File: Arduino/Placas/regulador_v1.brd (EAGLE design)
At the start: 5 parts

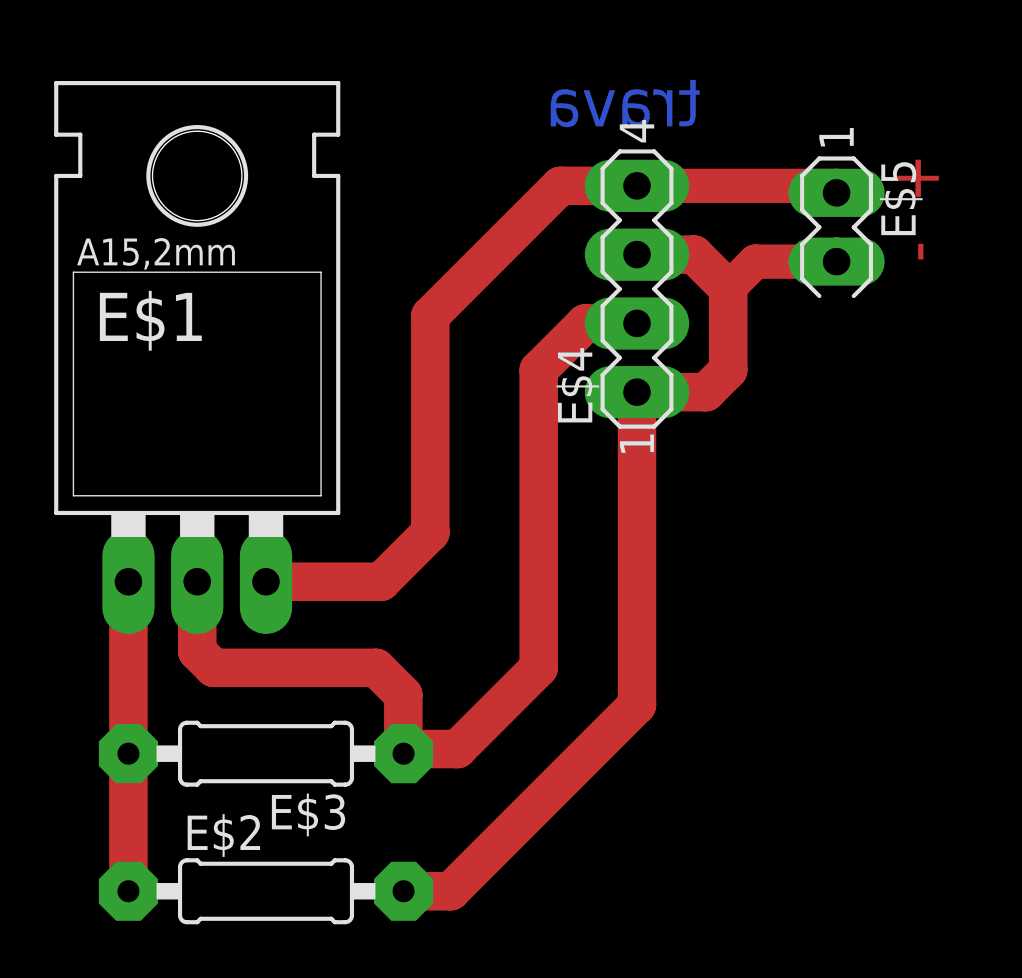
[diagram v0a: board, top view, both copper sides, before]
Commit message: Restored regulator board
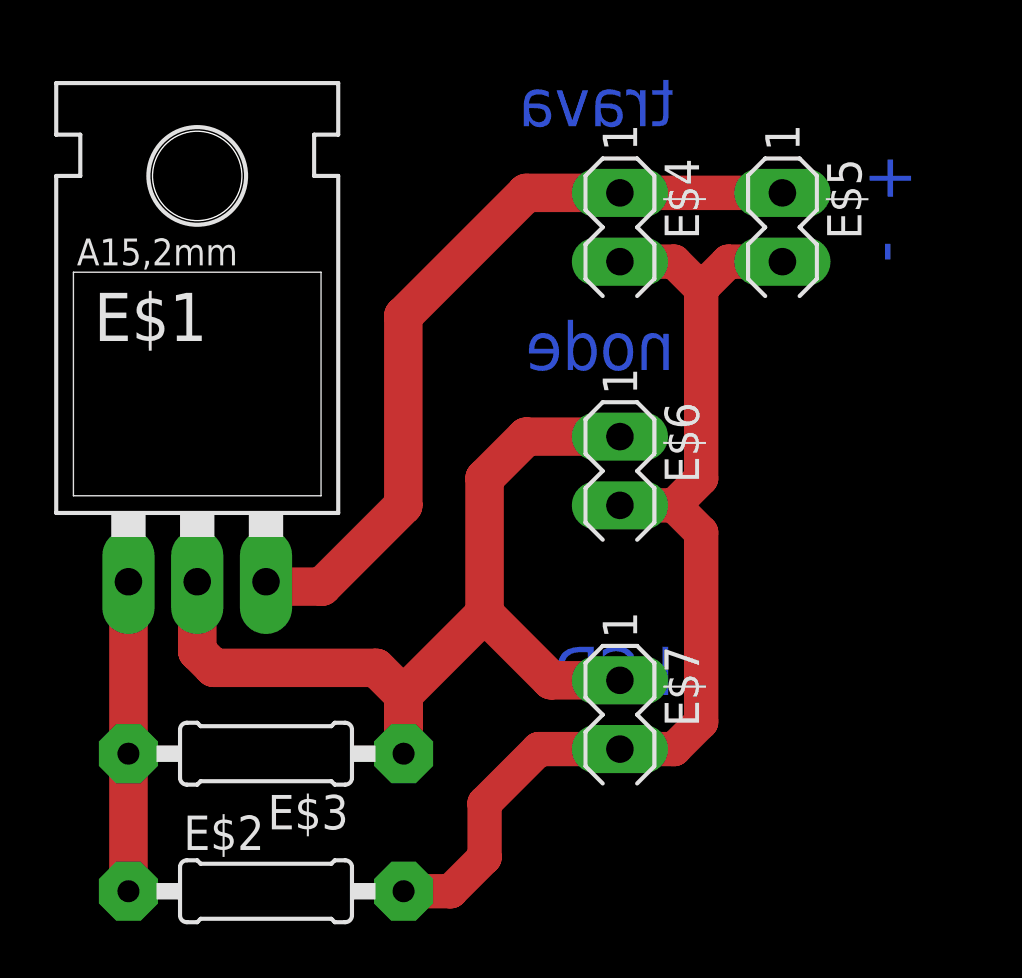
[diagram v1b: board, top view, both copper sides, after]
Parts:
- added E$6, E$7: (no value), con-lstb:MA03-1
- E$4: device con-lstb:MA04-1 -> con-lstb:MA03-1
- moved E$5 2.00 mm to (94.0, 55.0)
- moved E$4 1.19 mm to (88.0, 55.0), turned to 270 degrees
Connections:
- net S$2: now also E$6.1, E$7.1; no longer E$4.2
- net S$3: now also E$4.2, E$6.2, E$7.2; no longer E$4.1, E$4.3, E$5.2
- net S$4: now also E$4.1; no longer E$4.4
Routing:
- net S$4: track 32.1 -> 29.3 mm
- net S$3: track 38.4 -> 40.4 mm
- net S$2: track 34.5 -> 36.2 mm
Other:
- board text added: "LCD"
- board text added: "node"
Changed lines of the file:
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@@
 <board>
 <plain>
-<text x="98" y="59" size="1.778" layer="1" rot="R270">-  +</text>
-<text x="91" y="60" size="1.778" layer="16" rot="MR0">trava</text>
+<text x="90" y="60" size="1.778" layer="16" rot="MR0">trava</text>
+<text x="90" y="51" size="1.778" layer="16" rot="MR0">node</text>
+<text x="90" y="39" size="1.778" layer="16" rot="MR0">LCD
+</text>
+<text x="99" y="59" size="1.778" layer="16" rot="MR270">-  +</text>
 </plain>
 <attributes>
@@
 <element name="E$2" library="eagle-ltspice" package="0207/10" value="" x="74.93" y="31.75"/>
 <element name="E$3" library="eagle-ltspice" package="0207/10" value="" x="74.93" y="36.83" rot="R180"/>
-<element name="E$4" library="con-lstb" package="MA04-1" value="" x="88.63" y="53.99" rot="R90"/>
-<element name="E$5" library="con-lstb" package="MA03-1" value="" x="96" y="55" rot="R270"/>
+<element name="E$5" library="con-lstb" package="MA03-1" value="" x="94" y="55" rot="R270"/>
+<element name="E$4" library="con-lstb" package="MA03-1" value="" x="88" y="55" rot="R270"/>
+<element name="E$6" library="con-lstb" package="MA03-1" value="" x="88" y="46" rot="R270"/>
+<element name="E$7" library="con-lstb" package="MA03-1" value="" x="88" y="37" rot="R270"/>
 </elements>
 <signals>
@@
 <wire x1="69.85" y1="31.75" x2="69.85" y2="36.83" width="1.4224" layer="1"/>
 </signal>
+<signal name="S$4">
+<contactref element="E$5" pad="1"/>
+<contactref element="E$4" pad="1"/>
+<contactref element="E$1" pad="3"/>
+<wire x1="88" y1="57.54" x2="94" y2="57.54" width="1.27" layer="1"/>
+<wire x1="88" y1="57.54" x2="84.54" y2="57.54" width="1.4224" layer="1"/>
+<wire x1="84.54" y1="57.54" x2="80" y2="53" width="1.4224" layer="1"/>
+<wire x1="80" y1="53" x2="80" y2="46" width="1.4224" layer="1"/>
+<wire x1="80" y1="46" x2="77" y2="43" width="1.4224" layer="1"/>
+<wire x1="77" y1="43" x2="75.11" y2="43" width="1.4224" layer="1"/>
+<wire x1="75.11" y1="43" x2="74.93" y2="43.18" width="1.4224" layer="1"/>
+</signal>
 <signal name="S$2">
+<contactref element="E$6" pad="1"/>
+<wire x1="88" y1="48.54" x2="84.54" y2="48.54" width="1.4224" layer="1"/>
+<wire x1="83" y1="47" x2="84.54" y2="48.54" width="1.4224" layer="1"/>
+<wire x1="83" y1="42" x2="83" y2="47" width="1.4224" layer="1"/>
+<contactref element="E$3" pad="1"/>
+<wire x1="80.18" y1="37" x2="80.01" y2="36.83" width="1.4224" layer="1"/>
+<wire x1="80.01" y1="36.83" x2="80.01" y2="39.01" width="1.4224" layer="1"/>
+<wire x1="80.01" y1="39.01" x2="83" y2="42" width="1.4224" layer="1"/>
 <contactref element="E$1" pad="2"/>
-<contactref element="E$3" pad="1"/>
+<wire x1="80" y1="39" x2="80" y2="37" width="1.4224" layer="1"/>
+<wire x1="79" y1="40" x2="80" y2="39" width="1.4224" layer="1"/>
 <wire x1="72.39" y1="43.18" x2="72.39" y2="40.61" width="1.4224" layer="1"/>
 <wire x1="72.39" y1="40.61" x2="73" y2="40" width="1.4224" layer="1"/>
 <wire x1="73" y1="40" x2="79" y2="40" width="1.4224" layer="1"/>
-<wire x1="79" y1="40" x2="80" y2="39" width="1.4224" layer="1"/>
-<wire x1="80" y1="39" x2="80" y2="37" width="1.4224" layer="1"/>
+<contactref element="E$7" pad="1"/>
+<wire x1="88" y1="39.54" x2="85.46" y2="39.54" width="1.4224" layer="1"/>
+<wire x1="85.46" y1="39.54" x2="83" y2="42" width="1.4224" layer="1"/>
+<wire x1="80" y1="39" x2="80.01" y2="39.01" width="0" layer="19" extent="1-1"/>
+</signal>
+<signal name="S$3">
+<contactref element="E$6" pad="2"/>
 <contactref element="E$4" pad="2"/>
-<wire x1="88.63" y1="52.72" x2="86.72" y2="52.72" width="1.4224" layer="1"/>
-<wire x1="86.72" y1="52.72" x2="85" y2="51" width="1.4224" layer="1"/>
-<wire x1="85" y1="51" x2="85" y2="40" width="1.4224" layer="1"/>
-<wire x1="85" y1="40" x2="82" y2="37" width="1.4224" layer="1"/>
-<wire x1="82" y1="37" x2="80.18" y2="37" width="1.4224" layer="1"/>
-<wire x1="80.18" y1="37" x2="80.01" y2="36.83" width="1.4224" layer="1"/>
-<wire x1="80" y1="37" x2="80.01" y2="36.83" width="0" layer="19" extent="1-1"/>
-</signal>
-<signal name="S$3">
+<contactref element="E$7" pad="2"/>
 <contactref element="E$2" pad="2"/>
-<contactref element="E$4" pad="1"/>
-<wire x1="80.01" y1="31.75" x2="81.75" y2="31.75" width="1.4224" layer="1"/>
-<wire x1="81.75" y1="31.75" x2="88.63" y2="38.63" width="1.4224" layer="1"/>
-<wire x1="88.63" y1="50.18" x2="88.63" y2="38.63" width="1.4224" layer="1"/>
-<contactref element="E$4" pad="3"/>
-<wire x1="88.63" y1="50.18" x2="91.18" y2="50.18" width="1.4224" layer="1"/>
-<wire x1="91.18" y1="50.18" x2="92" y2="51" width="1.4224" layer="1"/>
-<wire x1="88.63" y1="55.26" x2="90.74" y2="55.26" width="1.4224" layer="1"/>
-<wire x1="90.74" y1="55.26" x2="92" y2="54" width="1.4224" layer="1"/>
-<wire x1="92" y1="54" x2="92" y2="51" width="1.4224" layer="1"/>
-<contactref element="E$5" pad="2"/>
-<wire x1="96" y1="55.26" x2="96" y2="55" width="1.27" layer="1"/>
-<wire x1="96" y1="55.26" x2="95.74" y2="55" width="1.27" layer="1"/>
-<wire x1="95.74" y1="55" x2="93" y2="55" width="1.27" layer="1"/>
-<wire x1="92" y1="54" x2="93" y2="55" width="1.27" layer="1"/>
-</signal>
-<signal name="S$4">
-<contactref element="E$4" pad="4"/>
-<contactref element="E$1" pad="3"/>
-<wire x1="74.93" y1="43.18" x2="79.18" y2="43.18" width="1.4224" layer="1"/>
-<wire x1="79.18" y1="43.18" x2="81" y2="45" width="1.4224" layer="1"/>
-<wire x1="88.63" y1="57.8" x2="85.8" y2="57.8" width="1.4224" layer="1"/>
-<wire x1="85.8" y1="57.8" x2="81" y2="53" width="1.4224" layer="1"/>
-<wire x1="81" y1="53" x2="81" y2="45" width="1.4224" layer="1"/>
-<contactref element="E$5" pad="1"/>
-<wire x1="88.63" y1="57.8" x2="96" y2="57.8" width="1.27" layer="1"/>
-<wire x1="96" y1="57.8" x2="96" y2="57.54" width="1.27" layer="1"/>
+<wire x1="80.01" y1="31.75" x2="81.75" y2="31.75" width="1.27" layer="1"/>
+<wire x1="81.75" y1="31.75" x2="83" y2="33" width="1.27" layer="1"/>
+<wire x1="88" y1="55" x2="90" y2="55" width="1.27" layer="1"/>
+<wire x1="90" y1="55" x2="91" y2="54" width="1.27" layer="1"/>
+<wire x1="91" y1="54" x2="91" y2="47" width="1.27" layer="1"/>
+<wire x1="91" y1="47" x2="90" y2="46" width="1.27" layer="1"/>
+<wire x1="90" y1="46" x2="88" y2="46" width="1.27" layer="1"/>
+<wire x1="88" y1="37" x2="85" y2="37" width="1.27" layer="1"/>
+<wire x1="85" y1="37" x2="83" y2="35" width="1.27" layer="1"/>
+<wire x1="83" y1="35" x2="83" y2="33" width="1.27" layer="1"/>
+<wire x1="88" y1="37" x2="90" y2="37" width="1.27" layer="1"/>
+<wire x1="90" y1="37" x2="91" y2="38" width="1.27" layer="1"/>
+<wire x1="91" y1="38" x2="91" y2="45" width="1.27" layer="1"/>
+<wire x1="91" y1="45" x2="90" y2="46" width="1.27" layer="1"/>
+<wire x1="91" y1="54" x2="92" y2="55" width="1.27" layer="1"/>
+<wire x1="92" y1="55" x2="94" y2="55" width="1.27" layer="1"/>
 </signal>
 </signals>
 </board>
 </drawing>
+<compatibility>
+<note version="6.3" minversion="6.2.2" severity="warning">
+Since Version 6.2.2 text objects can contain more than one line,
+which will not be processed correctly with this version.
+</note>
+</compatibility>
 </eagle>
